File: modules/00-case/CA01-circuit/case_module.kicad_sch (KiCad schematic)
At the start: 15 parts, among them J1 MODULE Connector, SW1 DummyBatteryCase

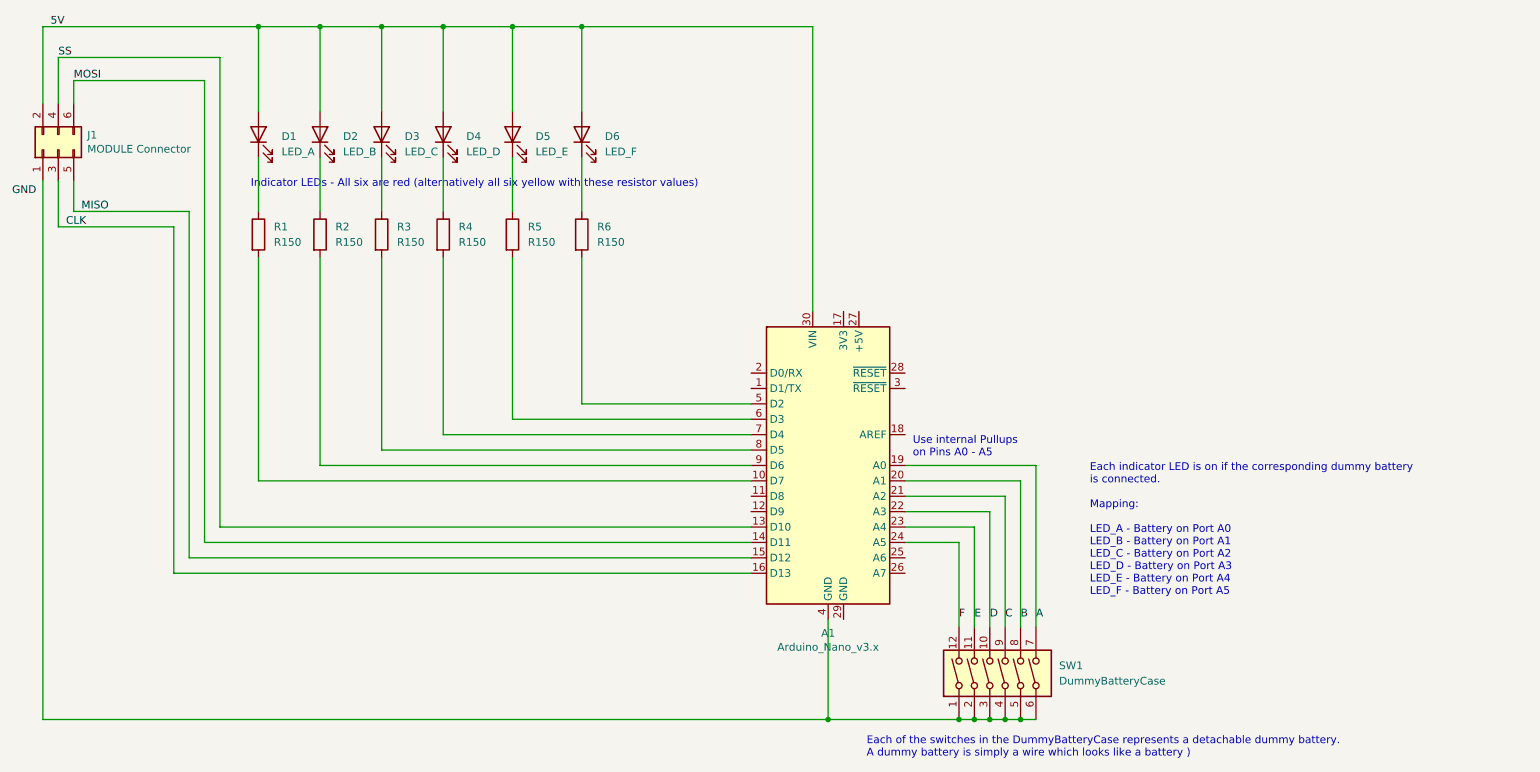
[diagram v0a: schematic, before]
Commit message: cleanup circuit
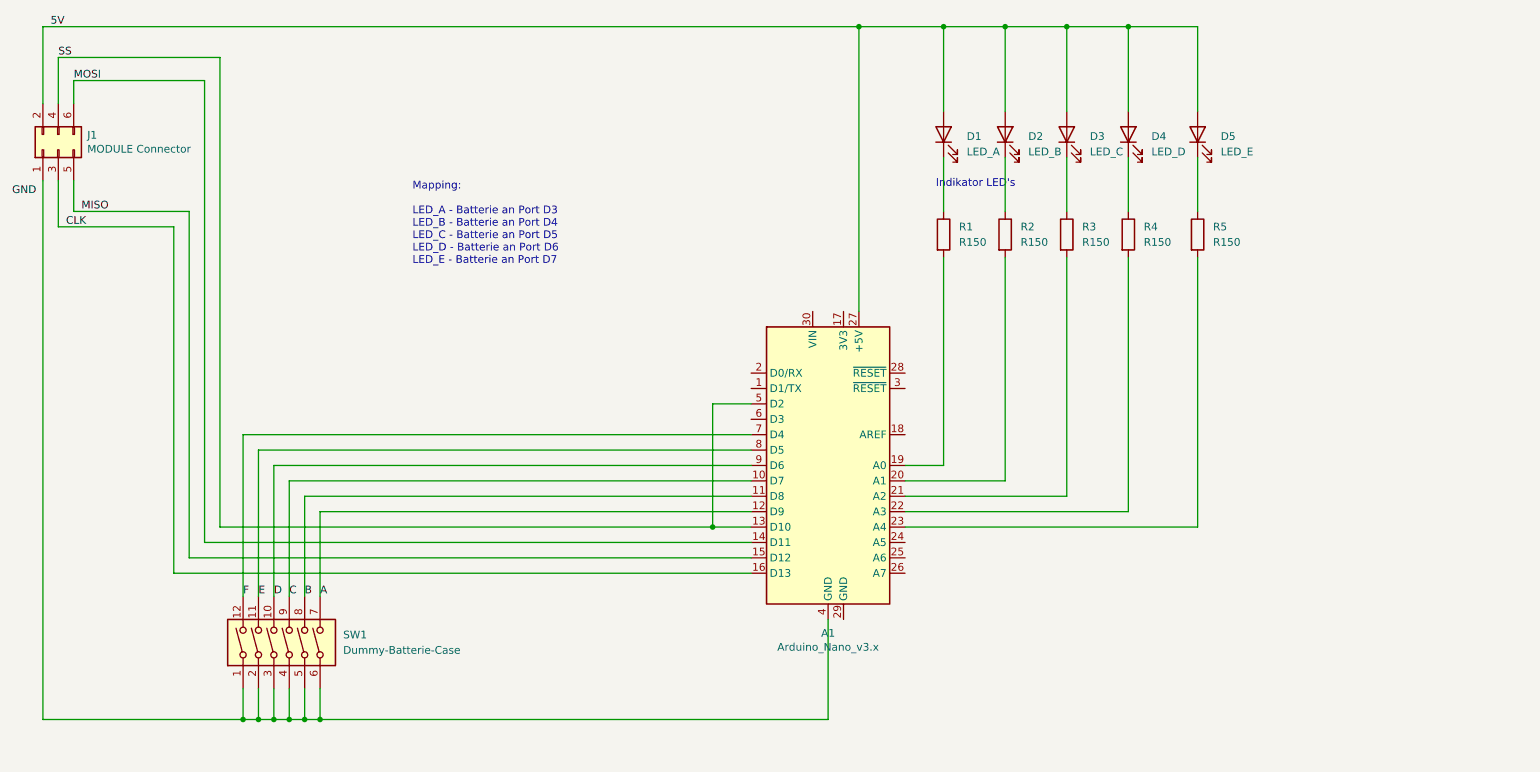
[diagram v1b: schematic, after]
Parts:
- removed D6: LED_F, symbol Device:LED
- removed R6: R150, symbol Device:R
- SW1: value DummyBatteryCase -> Dummy-Batterie-Case
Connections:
- net 5V: now also A1.27 (+5V); no longer A1.30 (VIN)
- net A: now also A1.12 (D9); no longer A1.19 (A0)
- net B: now also A1.11 (D8); no longer A1.20 (A1)
- net C: now also A1.10 (D7); no longer A1.21 (A2)
- net D: now also A1.9 (D6); no longer A1.22 (A3)
- net E: now also A1.8 (D5); no longer A1.23 (A4)
- net F: now also A1.7 (D4); no longer A1.24 (A5)
- net SS: now also A1.5 (D2)
- net at R1.2: now also A1.19 (A0); no longer A1.10 (D7)
- net at R5.2: now also A1.23 (A4); no longer A1.6 (D3)
- net at R4.2: now also A1.22 (A3); no longer A1.7 (D4)
- net at R3.2: now also A1.21 (A2); no longer A1.8 (D5)
- net at R2.2: now also A1.20 (A1); no longer A1.9 (D6)
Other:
- note added: "Indikator LED's"
- note added: "Mapping: LED_A - Batterie an Port D3 LED_B - Batterie an Port D4 LED_C - Batterie an Port D5 LED_D - Batterie an Port D6 LED_E - Batterie an Port D7"
- note removed: "Each indicator LED is on if the corresponding dummy battery is connected. Mapping: LED_A - Battery on Port A0 LED_B - Battery on Port A1 LED_C - Battery on Port A2 LED_D - Battery on Port A3 LED_E - Battery on Port A4 LED_F - Battery on Port A5"
- note removed: "Each of the switches in the DummyBatteryCase represents a detachable dummy battery. A dummy battery is simply a wire which looks like a battery )"
- note removed: "Indicator LEDs - All six are red (alternatively all six yellow with these resistor values)"
- note removed: "Use internal Pullups on Pins A0 - A5"
- title: (none) -> Schaltplan Modul Case (00)
- moved on the sheet: D1, D2, D3, D4, D5, R1, R2, R3, R4, R5, SW1
